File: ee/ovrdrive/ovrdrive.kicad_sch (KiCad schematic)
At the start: 43 parts, among them J1 USB_A, J2 Conn_01x02_Female, J3 AVR-ISP-6, Q1 Q_NMOS_DGS, U1 SM3257ENT, U2 FLASH, U3 ATtiny24A-MM, U4 74AUC1G32, U5 LMV321, U6 LM4040DBZ-2.5

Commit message: Initial routing complete.
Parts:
- removed J3: AVR-ISP-6, Connector_PinHeader_2.54mm:PinHeader_2x03_P2.54mm_Vertical_SMD, symbol Connector:AVR-ISP-6
- added TP1, TP2, TP3, TP4, TP5, TP6: TestPoint, TestPoint:TestPoint_Pad_1.0x1.0mm, symbol Connector:TestPoint
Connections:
- net +5V: now also TP1.1
- net GND: now also TP6.1
- net MISO: now also TP2.1
- net MOSI: now also TP3.1
- net SCK: now also TP4.1
- net ~{RST}: now also TP5.1
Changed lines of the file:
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@@
+    (stroke (width 0) (type default) (color 0 0 0 0))
+  )
+  (wire (pts (xy 48.26 151.765) (xy 52.705 151.765))
     (stroke (width 0) (type default) (color 0 0 0 0))
   )
@@
     (stroke (width 0) (type default) (color 0 0 0 0))
   )
-  (wire (pts (xy 35.56 142.24) (xy 35.56 146.685))
+  (wire (pts (xy 52.705 147.32) (xy 52.705 151.765))
     (stroke (width 0) (type default) (color 0 0 0 0))
   )
@@
     (stroke (width 0) (type default) (color 0 0 0 0))
   )
-  (wire (pts (xy 35.56 169.545) (xy 35.56 174.625))
+  (wire (pts (xy 52.705 164.465) (xy 52.705 170.18))
     (stroke (width 0) (type default) (color 0 0 0 0))
   )
@@
   )
   (wire (pts (xy 149.225 74.93) (xy 149.225 76.2))
+    (stroke (width 0) (type default) (color 0 0 0 0))
+  )
+  (wire (pts (xy 48.26 164.465) (xy 52.705 164.465))
     (stroke (width 0) (type default) (color 0 0 0 0))
   )
@@
     (pin "1")
   )
+  (symbol (lib_id "Connector:TestPoint") (at 48.26 156.845 90) (unit 1)
+    (in_bom yes) (on_board yes)
+    (property "Reference" "TP3" (id 0) (at 41.91 156.845 90))
+    (property "Value" "TestPoint" (id 1) (at 44.958 155.0471 90)
+      (effects (font (size 1.27 1.27)) hide)
+    )
+    (property "Footprint" "TestPoint:TestPoint_Pad_1.0x1.0mm" (id 2) (at 48.26 151.765 0)
+      (effects (font (size 1.27 1.27)) hide)
+    )
+    (property "Datasheet" "~" (id 3) (at 48.26 151.765 0)
+      (effects (font (size 1.27 1.27)) hide)
+    )
+    (pin "1")
+  )
   (symbol (lib_id "power:GND") (at 204.47 82.55 0) (unit 1)
     (in_bom yes) (on_board yes) (fields_autoplaced)
@@
     )
     (pin "1")
-  )
-  (symbol (lib_id "Connector:AVR-ISP-6") (at 38.1 159.385 0) (unit 1)
-    (in_bom yes) (on_board yes)
-    (property "Reference" "J3" (id 0) (at 42.545 145.415 0)
-      (effects (font (size 1.27 1.27)) (justify right))
-    )
-    (property "Value" "AVR-ISP-6" (id 1) (at 47.625 147.955 0)
-      (effects (font (size 1.27 1.27)) (justify right))
-    )
-    (property "Footprint" "Connector_PinHeader_2.54mm:PinHeader_2x03_P2.54mm_Vertical_SMD" (id 2) (at 31.75 158.115 90)
-      (effects (font (size 1.27 1.27)) hide)
-    )
-    (property "Datasheet" " ~" (id 3) (at 5.715 173.355 0)
-      (effects (font (size 1.27 1.27)) hide)
-    )
-    (pin "1")
-    (pin "2")
-    (pin "3")
-    (pin "4")
-    (pin "5")
-    (pin "6")
   )
   (symbol (lib_id "power:GND") (at 20.32 76.2 0) (unit 1)
@@
     (pin "2")
   )
+  (symbol (lib_id "Connector:TestPoint") (at 48.26 151.765 90) (unit 1)
+    (in_bom yes) (on_board yes)
+    (property "Reference" "TP1" (id 0) (at 41.91 151.765 90))
+    (property "Value" "TestPoint" (id 1) (at 44.958 149.9671 90)
+      (effects (font (size 1.27 1.27)) hide)
+    )
+    (property "Footprint" "TestPoint:TestPoint_Pad_1.0x1.0mm" (id 2) (at 48.26 146.685 0)
+      (effects (font (size 1.27 1.27)) hide)
+    )
+    (property "Datasheet" "~" (id 3) (at 48.26 146.685 0)
+      (effects (font (size 1.27 1.27)) hide)
+    )
+    (pin "1")
+  )
   (symbol (lib_id "power:GND") (at 60.96 66.675 0) (unit 1)
     (in_bom yes) (on_board yes)
@@
     (pin "1")
     (pin "2")
+  )
+  (symbol (lib_id "Connector:TestPoint") (at 48.26 161.925 90) (unit 1)
+    (in_bom yes) (on_board yes)
+    (property "Reference" "TP5" (id 0) (at 41.91 161.925 90))
+    (property "Value" "TestPoint" (id 1) (at 44.958 160.1271 90)
+      (effects (font (size 1.27 1.27)) hide)
+    )
+    (property "Footprint" "TestPoint:TestPoint_Pad_1.0x1.0mm" (id 2) (at 48.26 156.845 0)
+      (effects (font (size 1.27 1.27)) hide)
+    )
+    (property "Datasheet" "~" (id 3) (at 48.26 156.845 0)
+      (effects (font (size 1.27 1.27)) hide)
+    )
+    (pin "1")
+  )
+  (symbol (lib_id "Connector:TestPoint") (at 48.26 154.305 90) (unit 1)
+    (in_bom yes) (on_board yes)
+    (property "Reference" "TP2" (id 0) (at 41.91 154.305 90))
+    (property "Value" "TestPoint" (id 1) (at 44.958 152.5071 90)
+      (effects (font (size 1.27 1.27)) hide)
+    )
+    (property "Footprint" "TestPoint:TestPoint_Pad_1.0x1.0mm" (id 2) (at 48.26 149.225 0)
+      (effects (font (size 1.27 1.27)) hide)
+    )
+    (property "Datasheet" "~" (id 3) (at 48.26 149.225 0)
+      (effects (font (size 1.27 1.27)) hide)
+    )
+    (pin "1")
   )
   (symbol (lib_id "Device:R_Small_US") (at 34.925 59.055 90) (unit 1)
@@
     (pin "1")
   )
+  (symbol (lib_id "Connector:TestPoint") (at 48.26 159.385 90) (unit 1)
+    (in_bom yes) (on_board yes)
+    (property "Reference" "TP4" (id 0) (at 41.91 159.385 90))
+    (property "Value" "TestPoint" (id 1) (at 44.958 157.5871 90)
+      (effects (font (size 1.27 1.27)) hide)
+    )
+    (property "Footprint" "TestPoint:TestPoint_Pad_1.0x1.0mm" (id 2) (at 48.26 154.305 0)
+      (effects (font (size 1.27 1.27)) hide)
+    )
+    (property "Datasheet" "~" (id 3) (at 48.26 154.305 0)
+      (effects (font (size 1.27 1.27)) hide)
+    )
+    (pin "1")
+  )
   (symbol (lib_id "power:GND") (at 154.94 118.745 0) (unit 1)
     (in_bom yes) (on_board yes) (fields_autoplaced)
@@
     (pin "1")
   )
-  (symbol (lib_id "power:GND") (at 35.56 174.625 0) (unit 1)
-    (in_bom yes) (on_board yes)
-    (property "Reference" "#PWR025" (id 0) (at 35.56 180.975 0)
-      (effects (font (size 1.27 1.27)) hide)
-    )
-    (property "Value" "GND" (id 1) (at 35.56 178.435 0)
-      (effects (font (size 1.27 1.27)) hide)
-    )
-    (property "Footprint" "" (id 2) (at 35.56 174.625 0)
-      (effects (font (size 1.27 1.27)) hide)
-    )
-    (property "Datasheet" "" (id 3) (at 35.56 174.625 0)
+  (symbol (lib_id "power:GND") (at 52.705 170.18 0) (unit 1)
+    (in_bom yes) (on_board yes)
+    (property "Reference" "#PWR025" (id 0) (at 52.705 176.53 0)
+      (effects (font (size 1.27 1.27)) hide)
+    )
+    (property "Value" "GND" (id 1) (at 52.705 173.99 0)
+      (effects (font (size 1.27 1.27)) hide)
+    )
+    (property "Footprint" "" (id 2) (at 52.705 170.18 0)
+      (effects (font (size 1.27 1.27)) hide)
+    )
+    (property "Datasheet" "" (id 3) (at 52.705 170.18 0)
       (effects (font (size 1.27 1.27)) hide)
     )
@@
     (pin "4")
     (pin "5")
+  )
+  (symbol (lib_id "Connector:TestPoint") (at 48.26 164.465 90) (unit 1)
+    (in_bom yes) (on_board yes)
+    (property "Reference" "TP6" (id 0) (at 41.91 164.465 90))
+    (property "Value" "TestPoint" (id 1) (at 44.958 162.6671 90)
+      (effects (font (size 1.27 1.27)) hide)
+    )
+    (property "Footprint" "TestPoint:TestPoint_Pad_1.0x1.0mm" (id 2) (at 48.26 159.385 0)
+      (effects (font (size 1.27 1.27)) hide)
+    )
+    (property "Datasheet" "~" (id 3) (at 48.26 159.385 0)
+      (effects (font (size 1.27 1.27)) hide)
+    )
+    (pin "1")
   )
   (symbol (lib_id "Jumper:SolderJumper_2_Open") (at 52.07 118.11 90) (unit 1)
@@
     (pin "1")
   )
-  (symbol (lib_id "power:+5V") (at 35.56 142.24 0) (unit 1)
-    (in_bom yes) (on_board yes) (fields_autoplaced)
-    (property "Reference" "#PWR024" (id 0) (at 35.56 146.05 0)
-      (effects (font (size 1.27 1.27)) hide)
-    )
-    (property "Value" "+5V" (id 1) (at 35.56 138.6642 0))
-    (property "Footprint" "" (id 2) (at 35.56 142.24 0)
-      (effects (font (size 1.27 1.27)) hide)
-    )
-    (property "Datasheet" "" (id 3) (at 35.56 142.24 0)
+  (symbol (lib_id "power:+5V") (at 52.705 147.32 0) (unit 1)
+    (in_bom yes) (on_board yes) (fields_autoplaced)
+    (property "Reference" "#PWR024" (id 0) (at 52.705 151.13 0)
+      (effects (font (size 1.27 1.27)) hide)
+    )
+    (property "Value" "+5V" (id 1) (at 52.705 143.7442 0))
+    (property "Footprint" "" (id 2) (at 52.705 147.32 0)
+      (effects (font (size 1.27 1.27)) hide)
+    )
+    (property "Datasheet" "" (id 3) (at 52.705 147.32 0)
       (effects (font (size 1.27 1.27)) hide)
     )
@@
       (reference "J2") (unit 1) (value "Conn_01x02_Female") (footprint "")
     )
-    (path "/2c202c48-dc82-40bd-b46c-58a2374e8bfe"
-      (reference "J3") (unit 1) (value "AVR-ISP-6") (footprint "Connector_PinHeader_2.54mm:PinHeader_2x03_P2.54mm_Vertical_SMD")
-    )
     (path "/cb87ca4f-ba60-45c7-b41e-3ba96cfa29bc"
       (reference "JP1") (unit 1) (value "SolderJumper_2_Open") (footprint "Jumper:SolderJumper-2_P1.3mm_Open_Pad1.0x1.5mm")
@@
       (reference "R11") (unit 1) (value "2.2R") (footprint "Resistor_SMD:R_0603_1608Metric")
     )
+    (path "/4c76e122-53b6-43b3-8879-1a6cefbb40b5"
+      (reference "TP1") (unit 1) (value "TestPoint") (footprint "TestPoint:TestPoint_Pad_1.0x1.0mm")
+    )
+    (path "/65e988a0-9633-417f-8322-4d2dd4a6b7ce"
+      (reference "TP2") (unit 1) (value "TestPoint") (footprint "TestPoint:TestPoint_Pad_1.0x1.0mm")
+    )
+    (path "/23f0c802-29c6-4390-b8bd-c3adb8400e65"
+      (reference "TP3") (unit 1) (value "TestPoint") (footprint "TestPoint:TestPoint_Pad_1.0x1.0mm")
+    )
+    (path "/a211ba46-2089-4400-8db7-20892ea7f45c"
+      (reference "TP4") (unit 1) (value "TestPoint") (footprint "TestPoint:TestPoint_Pad_1.0x1.0mm")
+    )
+    (path "/6290be02-d754-4c67-873b-f8229b932a72"
+      (reference "TP5") (unit 1) (value "TestPoint") (footprint "TestPoint:TestPoint_Pad_1.0x1.0mm")
+    )
+    (path "/c00390ec-ff20-45e7-bb4f-2b147af99b44"
+      (reference "TP6") (unit 1) (value "TestPoint") (footprint "TestPoint:TestPoint_Pad_1.0x1.0mm")
+    )
     (path "/1a059912-e827-43c5-9c47-7ea3db4fc179"

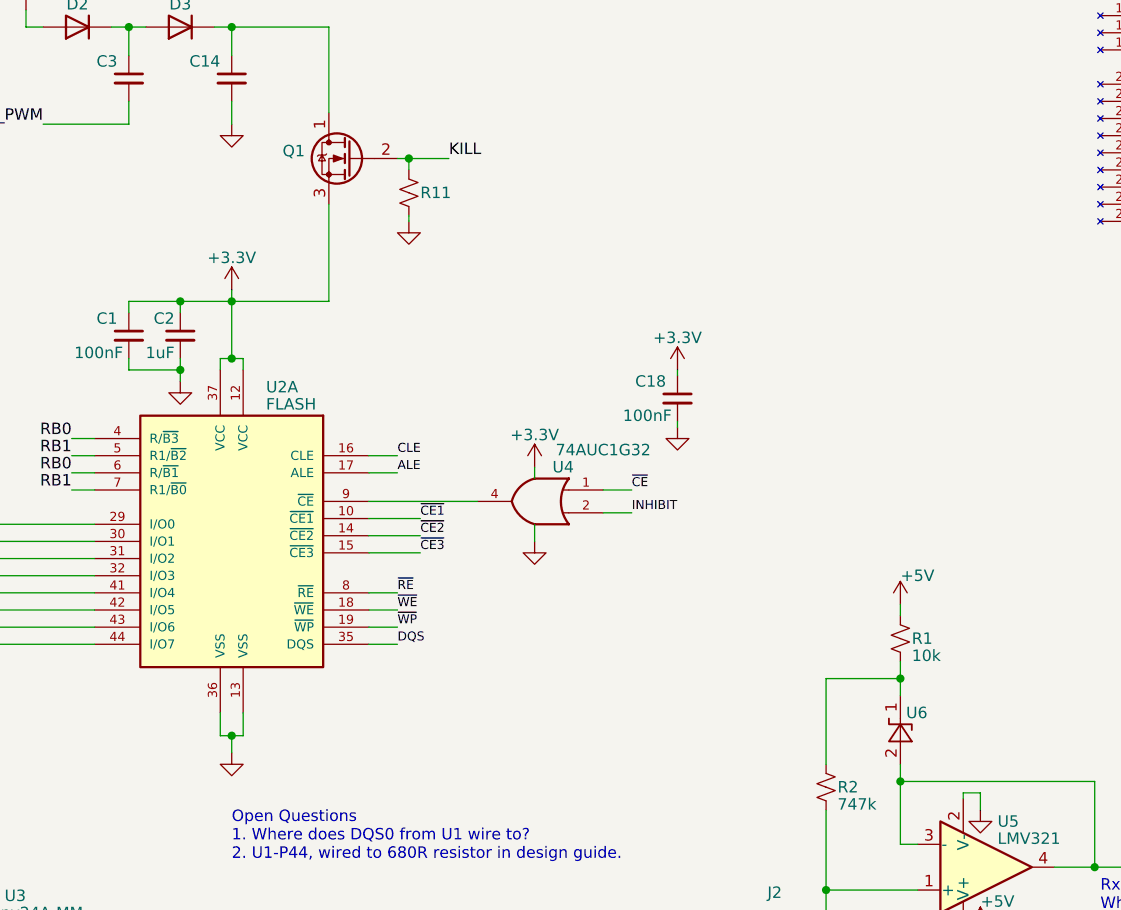
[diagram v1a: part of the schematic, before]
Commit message: Added some part numbers.
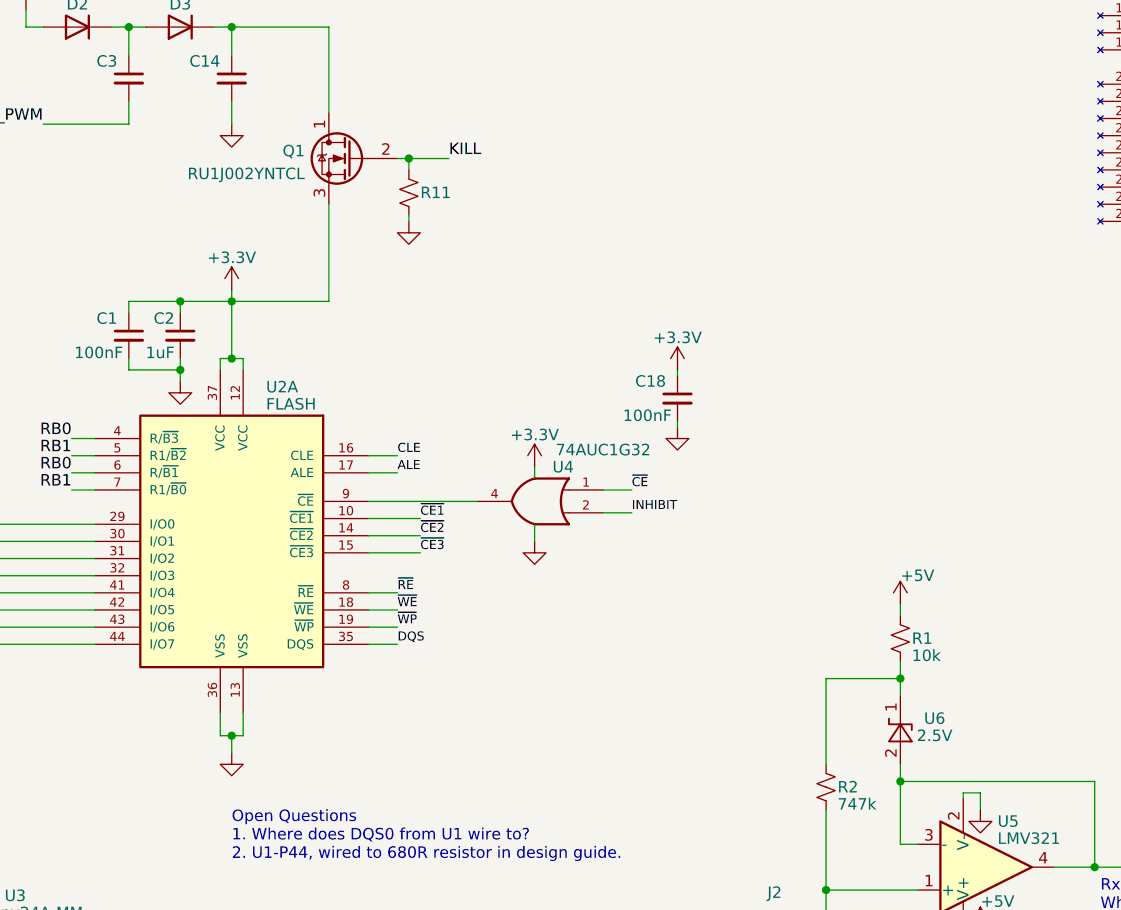
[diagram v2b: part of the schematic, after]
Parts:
- D1: MPN (none) -> XZMG53W-1
- D2, D3: MPN (none) -> CD0603-B0340R
- Q1: value Q_NMOS_DGS -> RU1J002YNTCL; MPN (none) -> RU1J002YNTCL
- R3, R4, R5: MPN (none) -> RK73B1JTTD2R2J
- U4: MPN (none) -> SN74AUC1G32DBVR
- U6: MPN (none) -> LM4040DBZ-2.5; Voltage (none) -> 2.5V
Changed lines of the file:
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@@
+      (effects (font (size 1.27 1.27)) hide)
+    )
+    (property "MPN" "RK73B1JTTD2R2J" (id 4) (at 34.925 59.055 90)
       (effects (font (size 1.27 1.27)) hide)
     )
@@
       (effects (font (size 1.27 1.27)) (justify left))
     )
-    (property "Value" "Q_NMOS_DGS" (id 1) (at 163.0681 54.4072 0)
-      (effects (font (size 1.27 1.27)) (justify left) hide)
+    (property "Value" "RU1J002YNTCL" (id 1) (at 163.0681 54.4072 0)
+      (effects (font (size 1.27 1.27)) (justify left))
     )
     (property "Footprint" "Package_TO_SOT_SMD:SOT-23" (id 2) (at 163.195 50.165 0)
@@
     )
     (property "Datasheet" "~" (id 3) (at 168.275 52.705 0)
+      (effects (font (size 1.27 1.27)) hide)
+    )
+    (property "MPN" "RU1J002YNTCL" (id 4) (at 168.275 52.705 0)
       (effects (font (size 1.27 1.27)) hide)
     )
@@
       (effects (font (size 1.27 1.27)) hide)
     )
+    (property "MPN" "RK73B1JTTD2R2J" (id 4) (at 34.925 61.595 90)
+      (effects (font (size 1.27 1.27)) hide)
+    )
     (pin "1")
     (pin "2")
@@
   (symbol (lib_id "Reference_Voltage:LM4040DBZ-2.5") (at 229.235 116.205 90) (unit 1)
     (in_bom yes) (on_board yes)
-    (property "Reference" "U6" (id 0) (at 229.87 114.3 90)
-      (effects (font (size 1.27 1.27)) (justify right))
-    )
+    (property "Reference" "U6" (id 0) (at 233.045 114.935 90))
     (property "Value" "LM4040DBZ-2.5" (id 1) (at 231.2416 117.9072 90)
       (effects (font (size 1.27 1.27)) (justify right) hide)
@@
       (effects (font (size 1.27 1.27) italic) hide)
     )
+    (property "MPN" "LM4040DBZ-2.5" (id 4) (at 229.235 116.205 90)
+      (effects (font (size 1.27 1.27)) hide)
+    )
+    (property "Voltage" "2.5V" (id 5) (at 233.045 116.84 90))
     (pin "1")
     (pin "2")
@@
     )
     (property "Datasheet" "~" (id 3) (at 149.225 38.1 0)
+      (effects (font (size 1.27 1.27)) hide)
+    )
+    (property "MPN" "CD0603-B0340R" (id 4) (at 149.225 38.1 0)
       (effects (font (size 1.27 1.27)) hide)
     )
@@
       (effects (font (size 1.27 1.27)) hide)
     )
+    (property "MPN" "SN74AUC1G32DBVR" (id 4) (at 188.595 90.805 0)
+      (effects (font (size 1.27 1.27)) hide)
+    )
     (pin "1")
     (pin "2")
@@
       (effects (font (size 1.27 1.27)) hide)
     )
+    (property "MPN" "XZMG53W-1" (id 4) (at 92.71 167.005 90)
+      (effects (font (size 1.27 1.27)) hide)
+    )
     (pin "1")
     (pin "2")
@@
     )
     (property "Datasheet" "~" (id 3) (at 34.925 53.975 0)
+      (effects (font (size 1.27 1.27)) hide)
+    )
+    (property "MPN" "RK73B1JTTD2R2J" (id 4) (at 34.925 53.975 90)
       (effects (font (size 1.27 1.27)) hide)
     )
@@
       (effects (font (size 1.27 1.27)) hide)
     )
+    (property "MPN" "CD0603-B0340R" (id 4) (at 137.795 38.1 0)
+      (effects (font (size 1.27 1.27)) hide)
+    )
     (pin "1")
     (pin "2")
@@
     )
     (path "/6cfd1694-ad72-4f07-aef7-23960c56a44c"
-      (reference "Q1") (unit 1) (value "Q_NMOS_DGS") (footprint "Package_TO_SOT_SMD:SOT-23")
+      (reference "Q1") (unit 1) (value "RU1J002YNTCL") (footprint "Package_TO_SOT_SMD:SOT-23")
     )
     (path "/a5438b38-e7f6-4919-9ac5-7e4362dd642e"
